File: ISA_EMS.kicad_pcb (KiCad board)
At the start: 2 copper layers, 104.1 x 102.9 mm, 41 parts, among them J1 ISA BUS, J2 EMS Address, U10 74HCT32, U11 74HCT04, U12 74ACT245, U17 74HCT138, U18 74HCT573, U19 74HCT573, U20 74HCT573, U21 74HCT573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

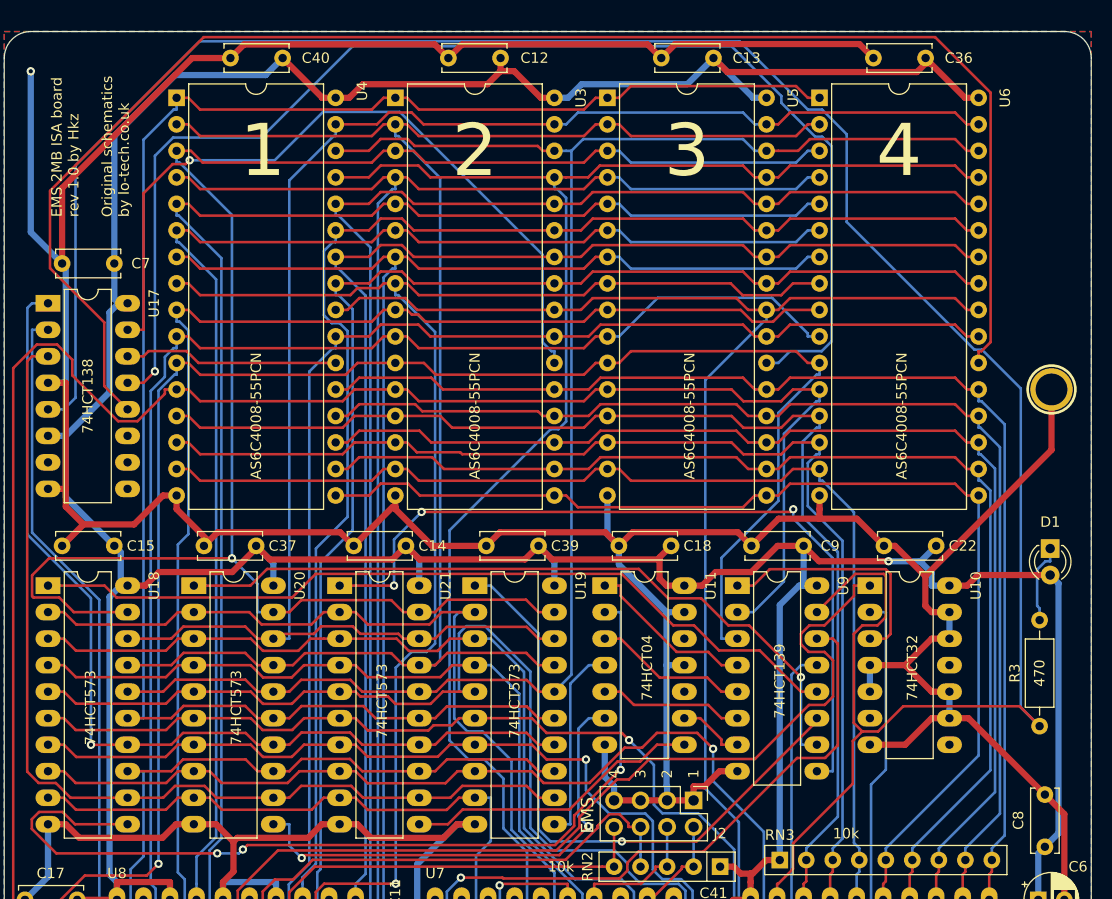
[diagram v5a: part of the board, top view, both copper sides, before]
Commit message: move led slightly backward
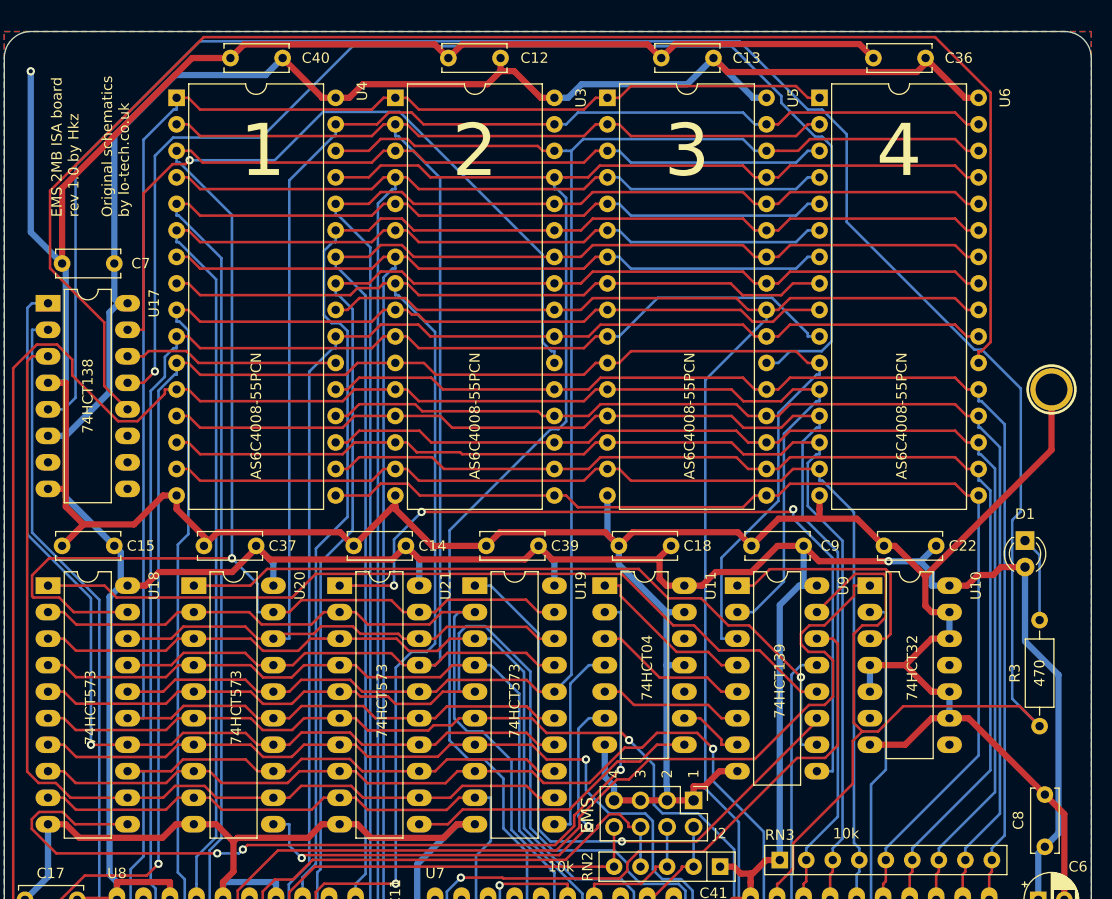
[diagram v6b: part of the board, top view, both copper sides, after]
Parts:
- moved D1 2.53 mm to (308.6, 149.1)
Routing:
- net /~RAM-SELECT: track 271.8 -> 272.5 mm
